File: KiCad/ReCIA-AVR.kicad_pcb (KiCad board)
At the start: 4 copper layers, 17.4 x 51.4 mm, 17 parts, among them U1 AVR128DA64-I_MR, U2 74AHCT1G17, U3 TLC2932AIPWR, U5 8520_DIP

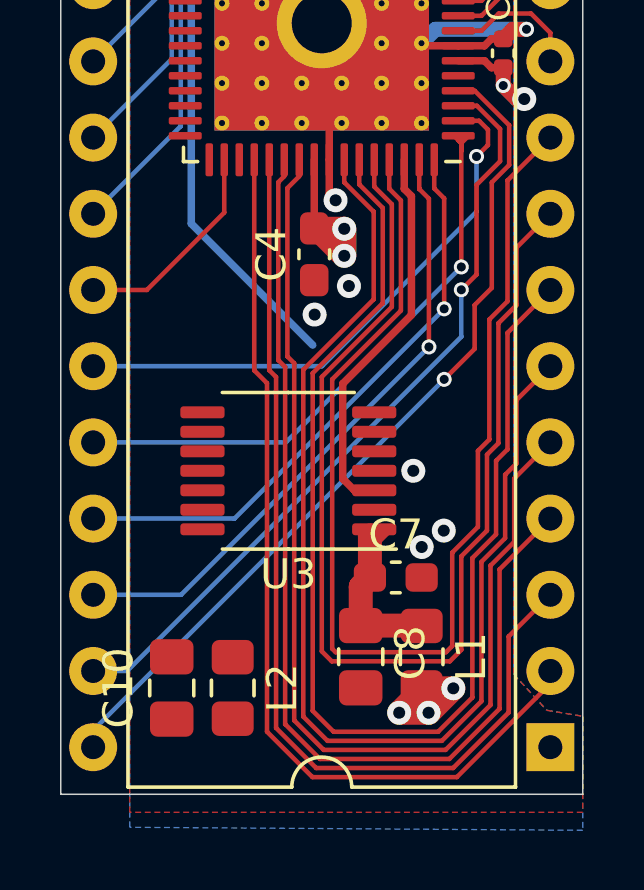
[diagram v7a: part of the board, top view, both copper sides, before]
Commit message: Add 33 Ohm damping resistor on EXTCLK-line
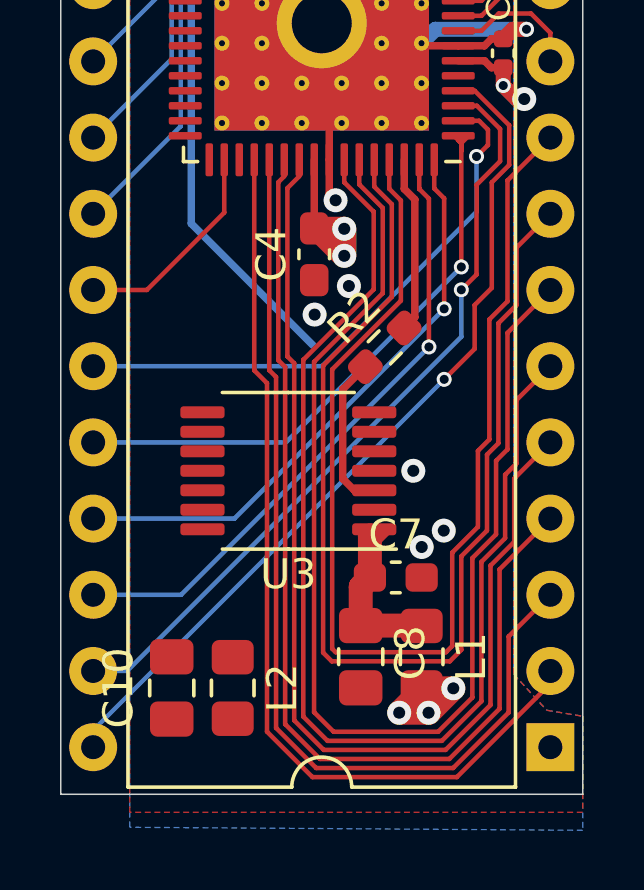
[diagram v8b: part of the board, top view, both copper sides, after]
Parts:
- added R2: 33, Resistor_SMD:R_0603_1608Metric_Pad0.98x0.95mm_HandSolder, F.Cu at (134.1, 93.8)
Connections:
- U3 pad 3: EXTCLK -> /EXT-CLK
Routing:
- net EXTCLK: track 12.9 -> 5.90 mm
- net /EXT-CLK: track 0.00 -> 5.26 mm
